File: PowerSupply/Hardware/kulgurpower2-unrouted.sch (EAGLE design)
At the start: 182 parts, among them M1 MST2V, M2 MST2V, M3 MST2V, M4 MST2V, Q1 IRLML6344TRPbF, Q2 IRLML6344TRPbF, Q3 IRLML6344TRPbF, Q4 IRLML6344TRPbF, X1 1727036, X2 2534-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

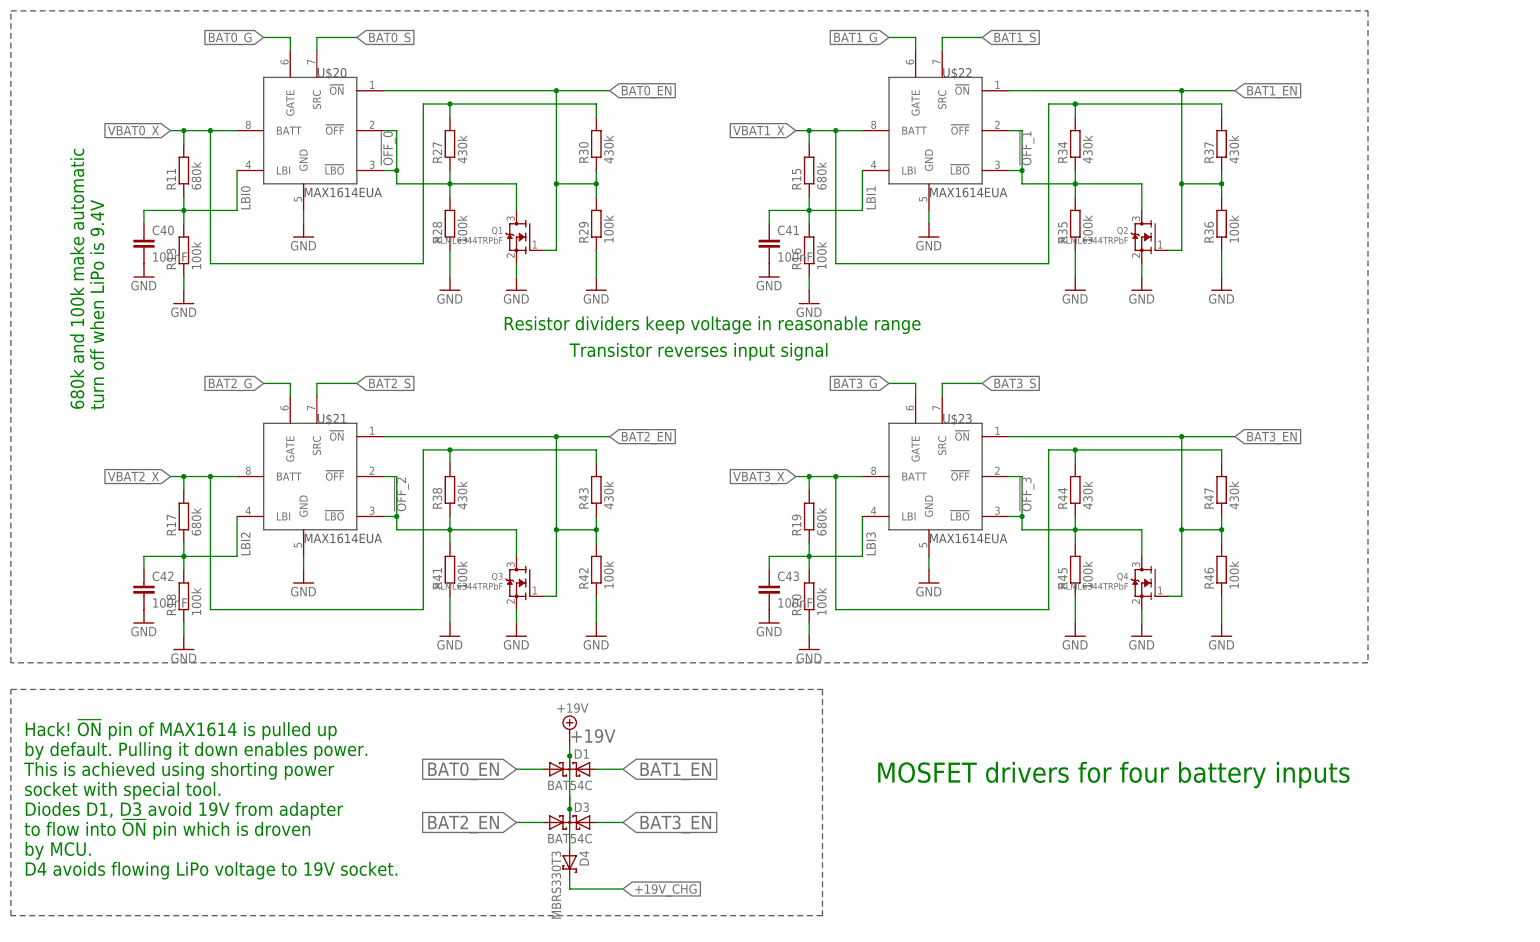
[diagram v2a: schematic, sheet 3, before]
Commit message: PCB/sch small changes. 19.2Mhz fix additional transistor PSU resistor fixes
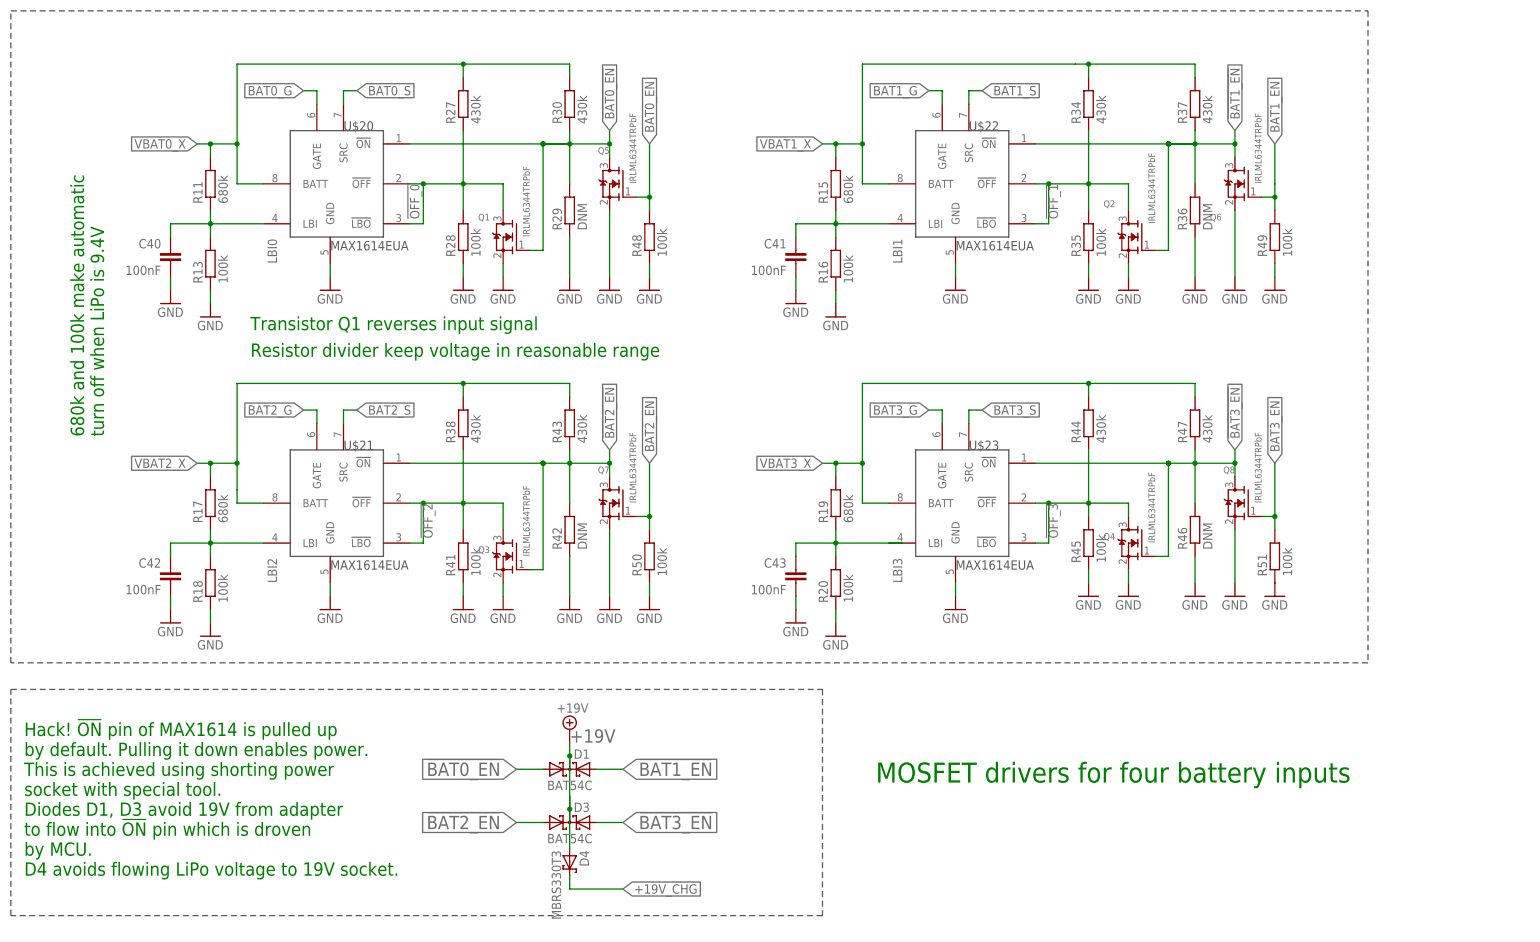
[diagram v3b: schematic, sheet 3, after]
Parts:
- added Q5, Q6, Q7, Q8: IRLML6344TRPbF, adafruit:MOSFET-NREFLOW
- added R48, R49, R50, R51: 100k, rcl:R-EU_R0603
- C13, C14, C44, C45: value 820uF/16V -> 820uF/25V
- C36, C37, C38: value 15V -> 47uF/25V
- C39: value 15v -> 47uF/25V
- F3, F4, F5, F6: value 10A FUSE 1206 -> 15A FUSE 1206
- R25: value 100k -> 3k12
- R29, R36, R42, R46: value 100k -> DNM
- R31: value 3k12 -> 10k
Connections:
- new net !BAT0_EN: D1.A1, Q1.G, Q5.D, R29.2, R30.1, U$20.!ON
- new net !BAT1_EN: D1.A2, Q2.G, Q6.D, R36.2, R37.1, U$22.!ON
- new net !BAT2_EN: D3.A1, Q3.G, Q7.D, R42.2, R43.1, U$21.!ON
- new net !BAT3_EN: D3.A2, Q4.G, Q8.D, R46.2, R47.1, U$23.!ON
- net BAT0_EN: now also Q5.G, R48.2; no longer D1.A1, Q1.G, R29.2, R30.1, U$20.!ON
- net BAT1_EN: now also Q6.G, R49.2; no longer D1.A2, Q2.G, R36.2, R37.1, U$22.!ON
- net BAT2_EN: now also Q7.G, R50.2; no longer D3.A1, Q3.G, R42.2, R43.1, U$21.!ON
- net BAT3_EN: now also Q8.G, R51.2; no longer D3.A2, Q4.G, R46.2, R47.1, U$23.!ON
- net GND: now also Q5.S, Q6.S, Q7.S, Q8.S, R48.1, R49.1, R50.1, R51.1
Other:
- note added: "Resistor divider keep voltage in reasonable range"
- note added: "Transistor Q1 reverses input signal"
- note removed: "Resistor dividers keep voltage in reasonable range"
- note removed: "Transistor reverses input signal"
- moved on the sheet: C40, C41, C42, C43, Q1, Q2, Q3, Q4, R11, R13, R15, R16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

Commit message: Values changed
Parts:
- R21: value 120k -> 180k
- R32: value 3k12 -> 10k
- R33: value 100k -> 3k12
- R40: value 270k -> 180k
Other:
- note added: "R1 = (VOUT -1.0) * R2 180 = 6 * 30"
- note removed: "R1 = (VOUT -1.0) * R2 120 = 4 * 30"
- note removed: "R1 = (VOUT -1.0) * R2 270 = 9 * 30"
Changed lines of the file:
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@@
 <part name="R4" library="rcl" deviceset="R-EU_" device="R0603" value="30k"/>
 <part name="R5" library="rcl" deviceset="R-EU_" device="R0603" value="30k"/>
-<part name="R21" library="rcl" deviceset="R-EU_" device="R0603" value="120k"/>
-<part name="R40" library="rcl" deviceset="R-EU_" device="R0603" value="270k"/>
+<part name="R21" library="rcl" deviceset="R-EU_" device="R0603" value="180k"/>
+<part name="R40" library="rcl" deviceset="R-EU_" device="R0603" value="180k"/>
 <part name="C5" library="rcl" deviceset="C-EU" device="C1210" value="10u"/>
 <part name="GND25" library="SparkFun" deviceset="GND" device=""/>
@@
 <part name="SJ104" library="rcl" deviceset="R-EU_" device="R0603" value="0R"/>
 <part name="R31" library="rcl" deviceset="R-EU_" device="R0603" value="10k"/>
-<part name="R32" library="rcl" deviceset="R-EU_" device="R0603" value="3k12"/>
+<part name="R32" library="rcl" deviceset="R-EU_" device="R0603" value="10k"/>
 <part name="R25" library="rcl" deviceset="R-EU_" device="R0603" value="3k12"/>
 <part name="C16" library="rcl" deviceset="C-EU" device="C0603" value="0,1u"/>
-<part name="R33" library="rcl" deviceset="R-EU_" device="R0603" value="100k"/>
+<part name="R33" library="rcl" deviceset="R-EU_" device="R0603" value="3k12"/>
 <part name="C20" library="rcl" deviceset="C-EU" device="C0603" value="0,1u"/>
 <part name="SJ114" library="rcl" deviceset="R-EU_" device="R0603" value="0R"/>
@@
 <text x="71.12" y="76.2" size="2.54" layer="91">5v 100mA</text>
 <text x="35.56" y="-12.7" size="1.778" layer="91">R1 = (VOUT -1.0) * R2
-120 = 4 * 30</text>
+180 = 6 * 30</text>
 <text x="109.22" y="-12.7" size="1.778" layer="91">R1 = (VOUT -1.0) * R2
-270 = 9 * 30</text>
+180 = 6 * 30</text>
 </plain>
 <instances>

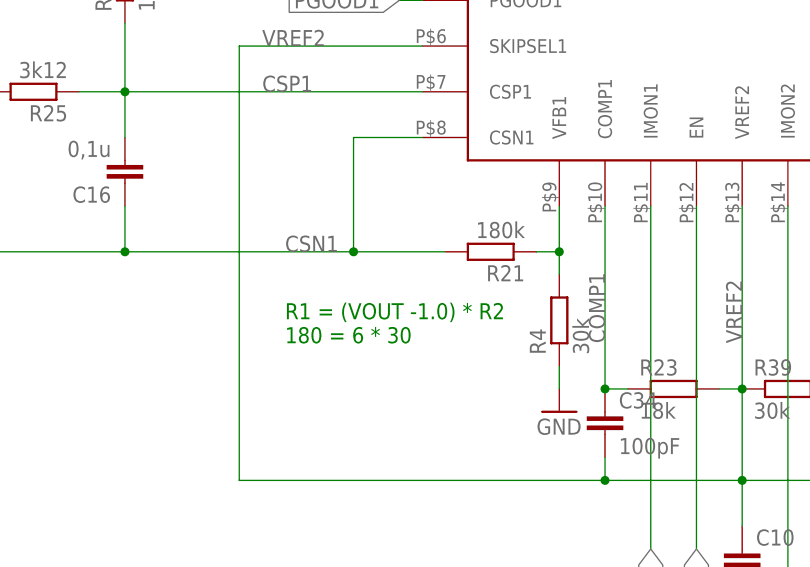
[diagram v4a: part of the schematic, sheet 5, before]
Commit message: 5V is important
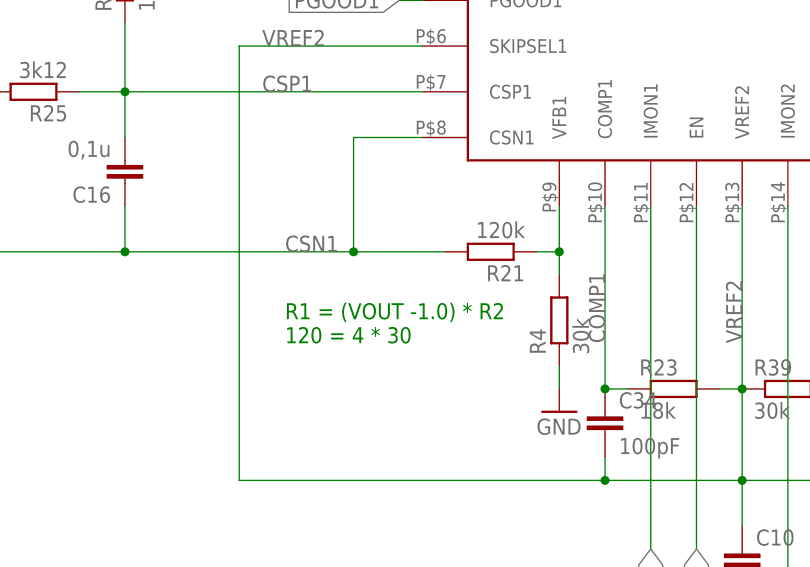
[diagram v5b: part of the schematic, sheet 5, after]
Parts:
- R21: value 180k -> 120k
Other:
- note added: "R1 = (VOUT -1.0) * R2 120 = 4 * 30"
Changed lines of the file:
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@@
 <part name="R4" library="rcl" deviceset="R-EU_" device="R0603" value="30k"/>
 <part name="R5" library="rcl" deviceset="R-EU_" device="R0603" value="30k"/>
-<part name="R21" library="rcl" deviceset="R-EU_" device="R0603" value="180k"/>
+<part name="R21" library="rcl" deviceset="R-EU_" device="R0603" value="120k"/>
 <part name="R40" library="rcl" deviceset="R-EU_" device="R0603" value="180k"/>
 <part name="C5" library="rcl" deviceset="C-EU" device="C1210" value="10u"/>
@@
 <text x="71.12" y="76.2" size="2.54" layer="91">5v 100mA</text>
 <text x="35.56" y="-12.7" size="1.778" layer="91">R1 = (VOUT -1.0) * R2
-180 = 6 * 30</text>
+120 = 4 * 30</text>
 <text x="109.22" y="-12.7" size="1.778" layer="91">R1 = (VOUT -1.0) * R2
 180 = 6 * 30</text>
